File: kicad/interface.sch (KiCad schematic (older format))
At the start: 33 parts, among them J1 BH-10(IDC-10MS), J2 PLS-2, J3 PBD-40(DS1023-2x20), J4 PLD-10(DS1021-2x5), U1 CAT24C32WI, U10 ASEMB-25.000MHZ-LC-T, U2 NUP4114UPXV6T1G, U3 NB3L553MNR, U7 10CL025ZE144

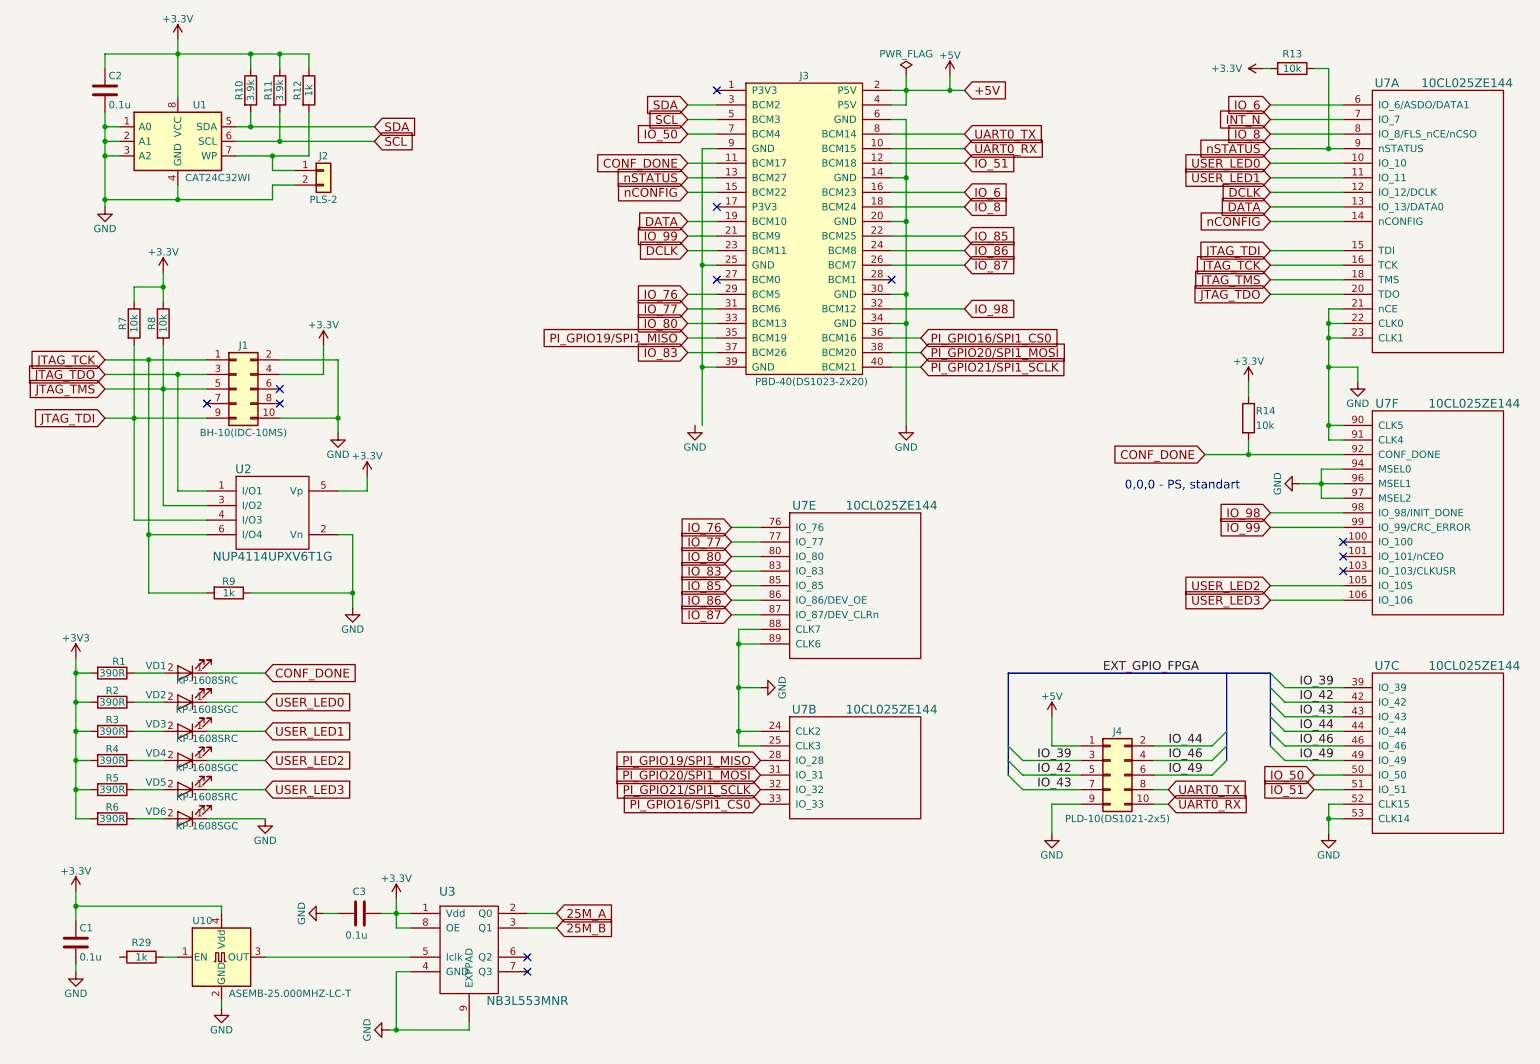
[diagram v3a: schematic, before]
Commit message: Corrected path for schematics Renumbered components Remaped GMII connections to other banks PCB updated - final placement for major components and some conn routed Corrected 3d models Add text Cyclone 10LP Added 3d models for new components Added folder assy (empty) Added folder bom Added BOM file (bom/BOM_fpgagigepi.xls)
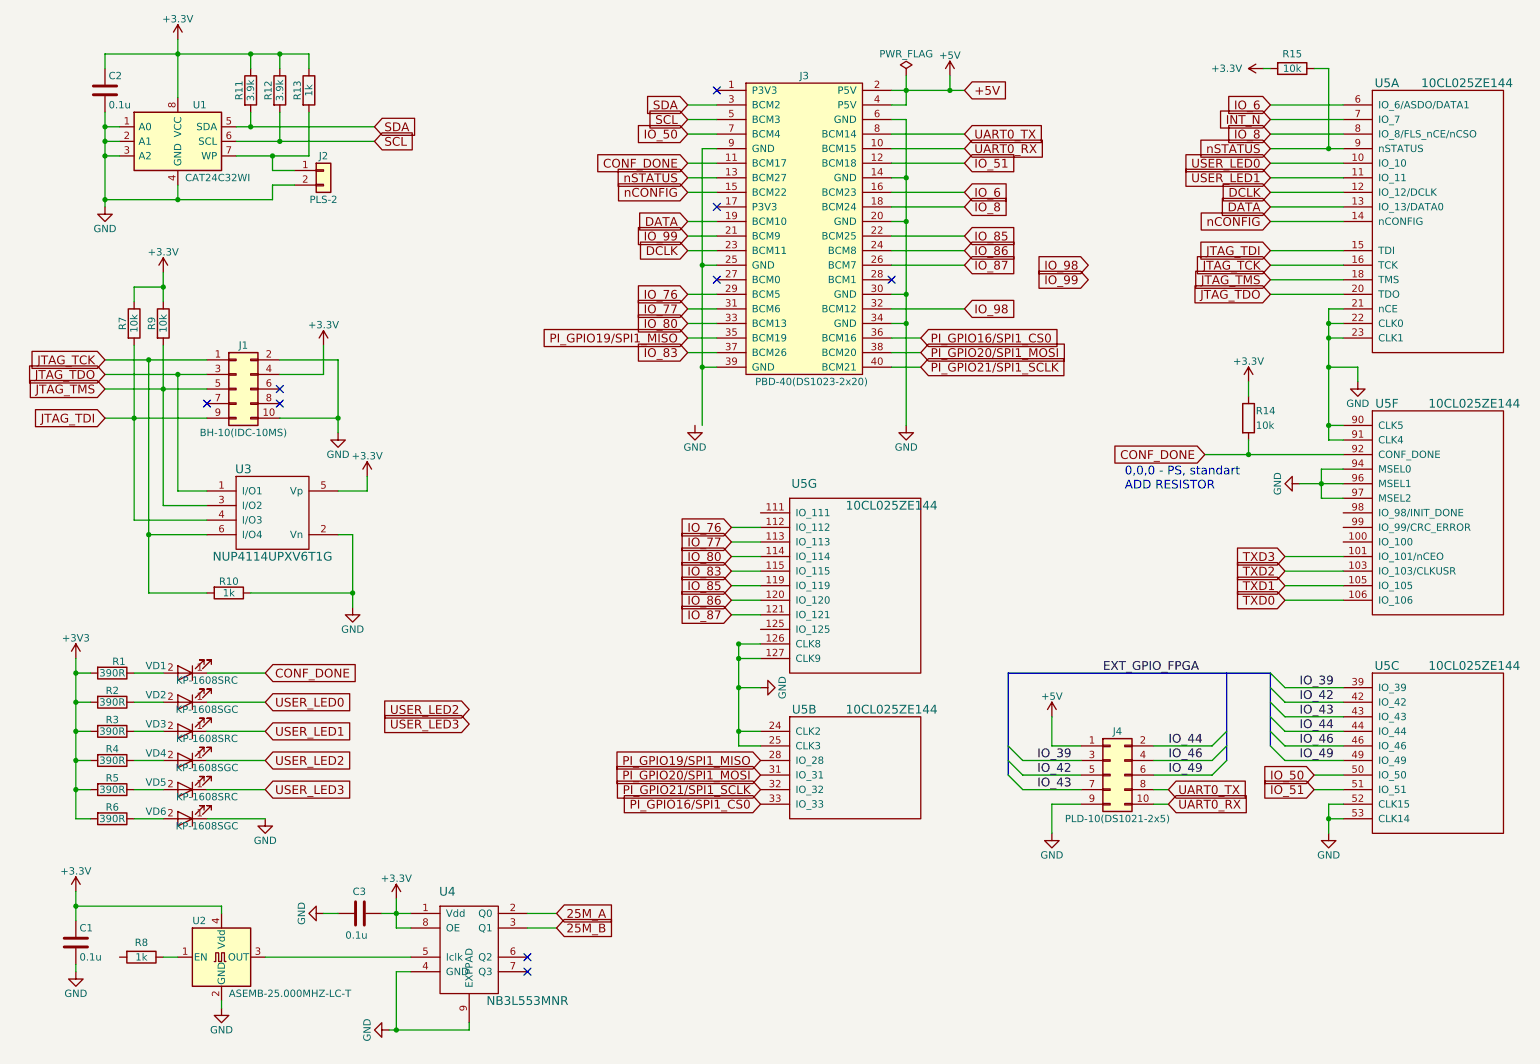
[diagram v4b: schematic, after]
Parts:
- renumbered R9 to R10, R10 to R11, R11 to R12, R12 to R13, R13 to R15, R29 to R8, R8 to R9, U10 to U2, U2 to U3, U3 to U4, U7 to U5
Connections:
- net GND: now also U5.126 (CLK8), U5.127 (CLK9); no longer U5.88 (CLK7), U5.89 (CLK6)
- net IO_76: now also U5.112 (IO_112); no longer U5.76 (IO_76)
- net IO_77: now also U5.113 (IO_113); no longer U5.77 (IO_77)
- net IO_80: now also U5.114 (IO_114); no longer U5.80 (IO_80)
- net IO_83: now also U5.115 (IO_115); no longer U5.83 (IO_83)
- net IO_85: now also U5.119 (IO_119); no longer U5.85 (IO_85)
- net IO_86: now also U5.120 (IO_120); no longer U5.86 (IO_86/DEV_OE)
- net IO_87: now also U5.121 (IO_121); no longer U5.87 (IO_87/DEV_CLRn)
- net IO_98: no longer U5.98 (IO_98/INIT_DONE)
- net IO_99: no longer U5.99 (IO_99/CRC_ERROR)
- net USER_LED2: no longer U5.105 (IO_105)
- net USER_LED3: no longer U5.106 (IO_106)
- net TXD3: now reaches U5.101 (IO_101/nCEO)
- net TXD2: now reaches U5.103 (IO_103/CLKUSR)
- new net TXD0: U5.106 (IO_106)
- new net TXD1: U5.105 (IO_105)
- no-connect marks 12 -> 9
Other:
- note added: "0,0,0 - PS, standart\nADD RESISTOR\n"
- note removed: "0,0,0 - PS, standart"
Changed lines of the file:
@@
 EESchema Schematic File Version 2
-LIBS:74xgxx
-LIBS:74xx
-LIBS:ac-dc
-LIBS:actel
-LIBS:adc-dac
-LIBS:allegro
-LIBS:Altera
-LIBS:analog_devices
-LIBS:analog_switches
-LIBS:atmel
-LIBS:audio
-LIBS:battery_management
-LIBS:bbd
-LIBS:bosch
-LIBS:brooktre
-LIBS:cmos_ieee
-LIBS:cmos4000
 LIBS:conn
-LIBS:contrib
-LIBS:cypress
-LIBS:dc-dc
-LIBS:device
-LIBS:digital-audio
-LIBS:diode
-LIBS:display
-LIBS:dsp
-LIBS:elec-unifil
-LIBS:ESD_Protection
-LIBS:ftdi
-LIBS:gennum
-LIBS:graphic_symbols
-LIBS:hc11
-LIBS:infineon
-LIBS:intel
-LIBS:interface
-LIBS:intersil
-LIBS:ir
-LIBS:Lattice
-LIBS:leds
-LIBS:LEM
-LIBS:linear
-LIBS:logic_programmable
-LIBS:maxim
-LIBS:mechanical
-LIBS:memory
-LIBS:microchip
-LIBS:microchip_dspic33dsc
-LIBS:microchip_pic10mcu
-LIBS:microchip_pic12mcu
-LIBS:microchip_pic16mcu
-LIBS:microchip_pic18mcu
-LIBS:microchip_pic24mcu
-LIBS:microchip_pic32mcu
-LIBS:microcontrollers
-LIBS:modules
-LIBS:motor_drivers
-LIBS:motorola
-LIBS:motors
-LIBS:msp430
-LIBS:nordicsemi
-LIBS:nxp
-LIBS:nxp_armmcu
-LIBS:onsemi
-LIBS:opto
-LIBS:Oscillators
-LIBS:philips
-LIBS:power
-LIBS:Power_Management
-LIBS:powerint
-LIBS:pspice
-LIBS:references
-LIBS:regul
-LIBS:relays
-LIBS:rfcom
-LIBS:RFSolutions
-LIBS:sensors
-LIBS:silabs
-LIBS:siliconi
-LIBS:stm8
-LIBS:stm32
-LIBS:supertex
-LIBS:switches
-LIBS:texas
-LIBS:transf
-LIBS:transistors
-LIBS:triac_thyristor
-LIBS:ttl_ieee
-LIBS:valves
-LIBS:video
-LIBS:wiznet
-LIBS:Worldsemi
-LIBS:Xicor
-LIBS:xilinx
-LIBS:zetex
-LIBS:Zilog
-LIBS:10cl025
-LIBS:88e1512
-LIBS:cfps-73
-LIBS:ksz9021gn
-LIBS:ksz9021rl
-LIBS:l829-1j1t-43
-LIBS:my
-LIBS:nb3l553
-LIBS:nup4114upxv6t1g
-LIBS:tlv62080
 LIBS:fpgagigepi-cache
 EELAYER 25 0
@@
 $EndDescr
 $Comp
-L 10cl025 U7
+L 10cl025 U5
 U 1 1 5AD09E19
 P 10450 2000
-F 0 "U7" H 10100 2950 60  0000 C CNN
+F 0 "U5" H 10100 2950 60  0000 C CNN
 F 1 "10CL025ZE144" H 10650 2950 60  0000 C CNN
 F 2 "library:EQFP-144_20x20mm_Pitch0.5mm" H 9450 2350 60  0001 C CNN
@@
 $EndComp
 $Comp
-L 10cl025 U7
+L 10cl025 U5
 U 2 1 5AD09EC2
 P 6450 5800
-F 0 "U7" H 6100 6250 60  0000 C CNN
+F 0 "U5" H 6100 6250 60  0000 C CNN
 F 1 "10CL025ZE144" H 6700 6250 60  0000 C CNN
 F 2 "library:EQFP-144_20x20mm_Pitch0.5mm" H 5450 6150 60  0001 C CNN
@@
 $EndComp
 $Comp
-L 10cl025 U7
+L 10cl025 U5
 U 3 1 5AD09F07
 P 10450 5600
-F 0 "U7" H 10100 6150 60  0000 C CNN
+F 0 "U5" H 10100 6150 60  0000 C CNN
 F 1 "10CL025ZE144" H 10700 6150 60  0000 C CNN
 F 2 "library:EQFP-144_20x20mm_Pitch0.5mm" H 9450 5950 60  0001 C CNN
@@
 $EndComp
 $Comp
-L 10cl025 U7
-U 5 1 5AD09F80
+L 10cl025 U5
+U 7 1 5AD09F80
 P 6450 4500
-F 0 "U7" H 6100 5050 60  0000 C CNN
+F 0 "U5" H 6100 5200 60  0000 C CNN
 F 1 "10CL025ZE144" H 6700 5050 60  0000 C CNN
 F 2 "library:EQFP-144_20x20mm_Pitch0.5mm" H 5450 4850 60  0001 C CNN
 F 3 "" H 5450 4850 60  0001 C CNN
-	5    6450 4500
-	1    0    0    -1
-$EndComp
-$Comp
-L 10cl025 U7
-U 6 1 5AD09FE7
-P 10450 4000
-F 0 "U7" H 10100 4750 60  0000 C CNN
-F 1 "10CL025ZE144" H 10700 4750 60  0000 C CNN
-F 2 "library:EQFP-144_20x20mm_Pitch0.5mm" H 9450 4350 60  0001 C CNN
-F 3 "" H 9450 4350 60  0001 C CNN
-	6    10450 4000
+	7    6450 4500
 	1    0    0    -1
 $EndComp
@@
 $EndComp
 $Comp
-L R R10
+L R R11
 U 1 1 5AD4AE48
 P 2300 1100
-F 0 "R10" V 2250 1100 50  0000 C BNN
+F 0 "R11" V 2250 1100 50  0000 C BNN
 F 1 "3.9k" V 2300 1100 50  0000 C CNN
 F 2 "Resistors_SMD:R_0603" V 2230 1100 50  0001 C CNN
@@
 $EndComp
 $Comp
-L R R11
+L R R12
 U 1 1 5AD4AEB7
 P 2500 1100
-F 0 "R11" V 2450 1100 50  0000 C BNN
+F 0 "R12" V 2450 1100 50  0000 C BNN
 F 1 "3.9k" V 2500 1100 50  0000 C CNN
 F 2 "Resistors_SMD:R_0603" V 2430 1100 50  0001 C CNN
@@
 $EndComp
 $Comp
-L R R12
+L R R13
 U 1 1 5AD4AF04
 P 2700 1100
-F 0 "R12" V 2650 1100 50  0000 C BNN
+F 0 "R13" V 2650 1100 50  0000 C BNN
 F 1 "1k" V 2700 1100 50  0000 C CNN
 F 2 "Resistors_SMD:R_0603" V 2630 1100 50  0001 C CNN
@@
 $EndComp
 $Comp
-L R R8
+L R R9
 U 1 1 5AD4E650
 P 1700 2700
-F 0 "R8" V 1650 2700 50  0000 C BNN
+F 0 "R9" V 1650 2700 50  0000 C BNN
 F 1 "10k" V 1700 2700 50  0000 C CNN
 F 2 "Resistors_SMD:R_0603" V 1630 2700 50  0001 C CNN
@@
 $EndComp
 $Comp
-L R R9
+L R R10
 U 1 1 5AD4E76B
 P 2150 4550
-F 0 "R9" V 2100 4550 50  0000 C BNN
+F 0 "R10" V 2100 4550 50  0000 C BNN
 F 1 "1k" V 2150 4550 50  0000 C CNN
 F 2 "Resistors_SMD:R_0603" V 2080 4550 50  0001 C CNN
@@
 USER_LED1
 $Comp
-L NUP4114UPXV6T1G U2
+L NUP4114UPXV6T1G U3
 U 1 1 5AD80184
 P 2450 4000
-F 0 "U2" H 2250 4300 60  0000 C CNN
+F 0 "U3" H 2250 4300 60  0000 C CNN
 F 1 "NUP4114UPXV6T1G" H 2450 3700 60  0000 C CNN
 F 2 "library:SOT-563-6" H 2450 3950 60  0001 C CNN
@@
 $EndComp
 $Comp
-L NB3L553 U3
+L NB3L553 U4
 U 1 1 5AD801F3
 P 3800 6950
-F 0 "U3" H 3650 7300 60  0000 C CNN
+F 0 "U4" H 3650 7300 60  0000 C CNN
 F 1 "NB3L553MNR" H 4200 6550 60  0000 C CNN
 F 2 "Housings_DFN_QFN:DFN-8-1EP_2x2mm_Pitch0.5mm" H 3800 6950 60  0001 C CNN
@@
 $EndComp
 $Comp
-L R R13
+L R R15
 U 1 1 5AD81C66
 P 9450 950
-F 0 "R13" V 9350 950 50  0000 C CNN
+F 0 "R15" V 9350 950 50  0000 C CNN
 F 1 "10k" V 9450 950 50  0000 C CNN
 F 2 "Resistors_SMD:R_0603" V 9380 950 50  0001 C CNN
@@
 $EndComp
 Text Notes 8300 3850 0    60   ~ 0
-0,0,0 - PS, standart
+0,0,0 - PS, standart\nADD RESISTOR\n
 Text GLabel 6900 2800 2    60   Input ~ 0
 PI_GPIO16/SPI1_CS0
@@
 Text GLabel 7200 2600 2    60   Input ~ 0
 IO_98
-Text GLabel 9300 4000 0    60   Input ~ 0
+Text GLabel 8050 2300 0    60   Input ~ 0
 IO_98
-NoConn ~ 9800 4200
-NoConn ~ 9800 4300
-NoConn ~ 9800 4400
-Text GLabel 9300 4100 0    60   Input ~ 0
+Text GLabel 8050 2400 0    60   Input ~ 0
 IO_99
 Text GLabel 5300 2100 0    60   Input ~ 0
@@
 	-1   0    0    1
 $EndComp
-Text GLabel 9300 4500 0    60   Input ~ 0
+Text GLabel 3800 5350 0    60   Input ~ 0
 USER_LED2
-Text GLabel 9300 4600 0    60   Input ~ 0
+Text GLabel 3800 5450 0    60   Input ~ 0
 USER_LED3
 $Comp
@@
 $EndComp
 $Comp
-L ASE-xxxMHz U10
+L ASE-xxxMHz U2
 U 1 1 5B11DC0F
 P 2100 7050
-F 0 "U10" H 1900 7300 50  0000 L CNN
+F 0 "U2" H 1900 7300 50  0000 L CNN
 F 1 "ASEMB-25.000MHZ-LC-T" H 2150 6800 50  0000 L CNN
 F 2 "Oscillators:Oscillator_SMD_Abracon_ASE-4pin_3.2x2.5mm" H 2800 6700 50  0001 C CNN
@@
 $EndComp
 $Comp
-L R R29
+L R R8
 U 1 1 5B11FA29
 P 1550 7050
-F 0 "R29" V 1450 7050 50  0000 C CNN
+F 0 "R8" V 1450 7050 50  0000 C CNN
 F 1 "1k" V 1550 7050 50  0000 C CNN
 F 2 "Resistors_SMD:R_0603" V 1480 7050 50  0001 C CNN
@@
 	6700 2800 6900 2800
 Wire Wire Line
-	5800 4800 5650 4800
-Wire Wire Line
-	5650 4800 5650 5600
+	5650 4900 5650 5600
 Wire Wire Line
 	5650 5600 5800 5600
@@
 	5800 4100 5600 4100
 Wire Wire Line
-	9800 4000 9300 4000
-Wire Wire Line
-	9300 4100 9800 4100
-Wire Wire Line
 	2400 5700 2000 5700
 Wire Wire Line
@@
 Connection ~ 1100 5900
 Wire Wire Line
-	9300 4500 9800 4500
-Wire Wire Line
-	9800 4600 9300 4600
-Wire Wire Line
 	3250 7550 3800 7550
 Wire Wire Line
@@
 Wire Wire Line
 	2700 850  2700 950
+$Comp
+L 10cl025 U5
+U 6 1 5AD09FE7
+P 10450 4000
+F 0 "U5" H 10100 4750 60  0000 C CNN
+F 1 "10CL025ZE144" H 10700 4750 60  0000 C CNN
+F 2 "library:EQFP-144_20x20mm_Pitch0.5mm" H 9450 4350 60  0001 C CNN
+F 3 "" H 9450 4350 60  0001 C CNN
+	6    10450 4000
+	1    0    0    -1
+$EndComp
+Text GLabel 9400 4600 0    60   Input ~ 0
+TXD0
+Text GLabel 9400 4500 0    60   Input ~ 0
+TXD1
+Text GLabel 9400 4400 0    60   Input ~ 0
+TXD2
+Text GLabel 9400 4300 0    60   Input ~ 0
+TXD3
+Wire Wire Line
+	9400 4300 9800 4300
+Wire Wire Line
+	9400 4400 9800 4400
+Wire Wire Line
+	9400 4500 9800 4500
+Wire Wire Line
+	9800 4600 9400 4600
+Wire Wire Line
+	5800 5000 5650 5000
+Connection ~ 5650 5000
 $EndSCHEMATC

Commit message: Replaced clock buffer NB3L553DR2G to cdclvc1102 Added datasheet for cdclvc1102 Added components cdclvc1102pw in library_cache Remaped cyclone-to-40-pin-header connections Updated schematics Updated PCB - all signal routed. Power connections not routed Updated BOM file (non-altium format)
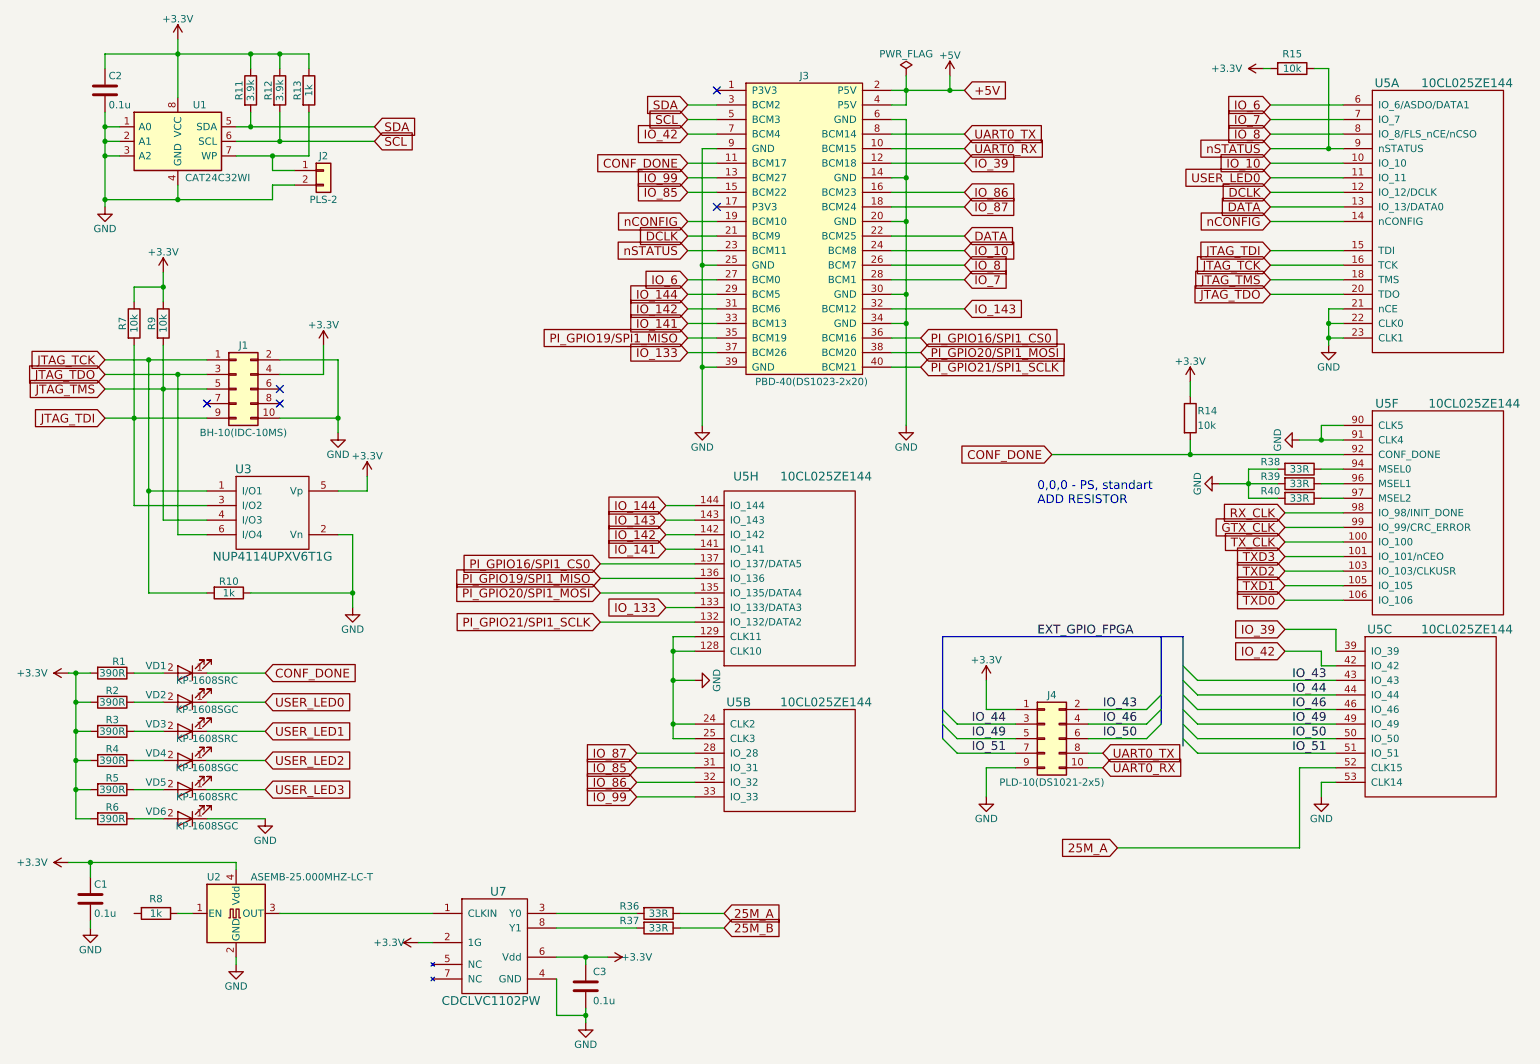
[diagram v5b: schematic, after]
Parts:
- removed U4: NB3L553MNR, Housings_DFN_QFN:DFN-8-1EP_2x2mm_Pitch0.5mm, symbol NB3L553
- added R36, R37, R38, R39, R40: 33R, Resistors_SMD:R_0603, symbol R
- added U7: CDCLVC1102PW, Housings_SSOP:TSSOP-8_4.4x3mm_Pitch0.65mm, symbol CDCLVC1102PW
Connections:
- net INT_N is gone; now on net IO_7: U5.7 (IO_7)
- net +3V3: now also C3.2, J4.1 (Pin_1), U7.2 (1G), U7.6 (Vdd); no longer C3.1
- net +5V: no longer J4.1 (Pin_1)
- net 25M_A: now also U5.52 (CLK15), R36.1
- net 25M_B: now also R37.1
- net DATA: now also J3.22 (BCM25); no longer J3.19 (BCM10)
- net DCLK: now also J3.21 (BCM9); no longer J3.23 (BCM11)
- net GND: now also C3.1, J3.25 (GND), J3.39 (GND), J3.9 (GND), U5.128 (CLK10), U5.129 (CLK11), R38.2, R39.2, R40.2, U7.4 (GND); no longer C3.2, U5.126 (CLK8), U5.127 (CLK9), U5.52 (CLK15), U5.94 (MSEL0), U5.96 (MSEL1), U5.97 (MSEL2)
- net IO_39: now also J3.12 (BCM18); no longer J4.3 (Pin_3)
- net IO_42: now also J3.7 (BCM4); no longer J4.5 (Pin_5)
- net IO_43: now also J4.2 (Pin_2); no longer J4.7 (Pin_7)
- net IO_44: now also J4.3 (Pin_3); no longer J4.2 (Pin_2)
- net IO_49: now also J4.5 (Pin_5); no longer J4.6 (Pin_6)
- net IO_50: now also J4.6 (Pin_6); no longer J3.7 (BCM4)
- net IO_51: now also J4.7 (Pin_7); no longer J3.12 (BCM18)
- net IO_6: now also J3.27 (BCM0); no longer J3.16 (BCM23)
- net IO_8: now also J3.26 (BCM7); no longer J3.18 (BCM24)
- net IO_85: now also J3.15 (BCM22), U5.31 (IO_31); no longer J3.22 (BCM25), U5.119 (IO_119)
- net IO_86: now also J3.16 (BCM23), U5.32 (IO_32); no longer J3.24 (BCM8), U5.120 (IO_120)
- net IO_87: now also J3.18 (BCM24), U5.28 (IO_28); no longer J3.26 (BCM7), U5.121 (IO_121)
- net IO_99: now also J3.13 (BCM27), U5.33 (IO_33); no longer J3.21 (BCM9)
- net JTAG_TCK: now also U3.1 (I/O1); no longer U3.6 (I/O4)
- net JTAG_TDI: now also U3.3 (I/O2); no longer U3.4 (I/O3)
- net JTAG_TDO: now also U3.6 (I/O4); no longer U3.1 (I/O1)
- net JTAG_TMS: now also U3.4 (I/O3); no longer U3.3 (I/O2)
- net PI_GPIO16/SPI1_CS0: now also U5.137 (IO_137/DATA5); no longer U5.33 (IO_33)
- net PI_GPIO19/SPI1_MISO: now also U5.136 (IO_136); no longer U5.28 (IO_28)
- net PI_GPIO20/SPI1_MOSI: now also U5.135 (IO_135/DATA4); no longer U5.31 (IO_31)
- net PI_GPIO21/SPI1_SCLK: now also U5.132 (IO_132/DATA2); no longer U5.32 (IO_32)
- net USER_LED0: now also U5.11 (IO_11); no longer U5.10 (IO_10)
- net USER_LED1: no longer U5.11 (IO_11)
- net nCONFIG: now also J3.19 (BCM10); no longer J3.15 (BCM22)
- net nSTATUS: now also J3.23 (BCM11); no longer J3.13 (BCM27)
- net TX_CLK: now reaches U5.100 (IO_100)
- net RX_CLK: now reaches U5.98 (IO_98/INIT_DONE)
- net GTX_CLK: now reaches U5.99 (IO_99/CRC_ERROR)
- net at U2.3 (OUT): now also U7.1 (CLKIN)
- net IO_7: now reaches J3.28 (BCM1)
- net IO_76 renamed IO_144
- net IO_144: now also U5.144 (IO_144); no longer U5.112 (IO_112)
- net IO_77 renamed IO_142
- net IO_142: now also U5.142 (IO_142); no longer U5.113 (IO_113)
- net IO_80 renamed IO_141
- net IO_141: now also U5.141 (IO_141); no longer U5.114 (IO_114)
- net IO_83 renamed IO_133
- net IO_133: now also U5.133 (IO_133/DATA3); no longer U5.115 (IO_115)
- net IO_98 renamed IO_143
- net IO_143: now also U5.143 (IO_143)
- new net: R38.1, U5.94 (MSEL0)
- new net: R39.1, U5.96 (MSEL1)
- new net: R40.1, U5.97 (MSEL2)
- new net: R36.2, U7.3 (Y0)
- new net: R37.2, U7.8 (Y1)
- new net IO_10: J3.24 (BCM8), U5.10 (IO_10)
- no-connect marks 9 -> 5
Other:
- moved on the sheet: C1, C3, J4, R14, R8, U2, U5B, U5C
